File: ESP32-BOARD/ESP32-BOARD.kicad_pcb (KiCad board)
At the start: 2 copper layers, 150 x 99.9 mm, 160 parts, among them J101 Screw_Terminal_01x08, J102 Screw_Terminal_01x08, J103 Screw_Terminal_01x08, J104 Screw_Terminal_01x08, J105 Input_01x02, J106 Screw_Terminal_01x04, J120 Conn_01x07_Male, Q101 BT136-600, Q102 BT136-600, Q103 BT136-600, Q104 BT136-600, U101 LM358, U102 LM358, U103 LM2596S-ADJ, U104 LM2596S-ADJ, U105 TLP290-4, U106 TLP290-4, U107 KAQY212S, U108 KAQY212S, U109 MOC3023S, U110 MOC3023S, U111 MOC3023S, U112 MOC3023S, U113 SIM800L, U114 ESP32-dev-board

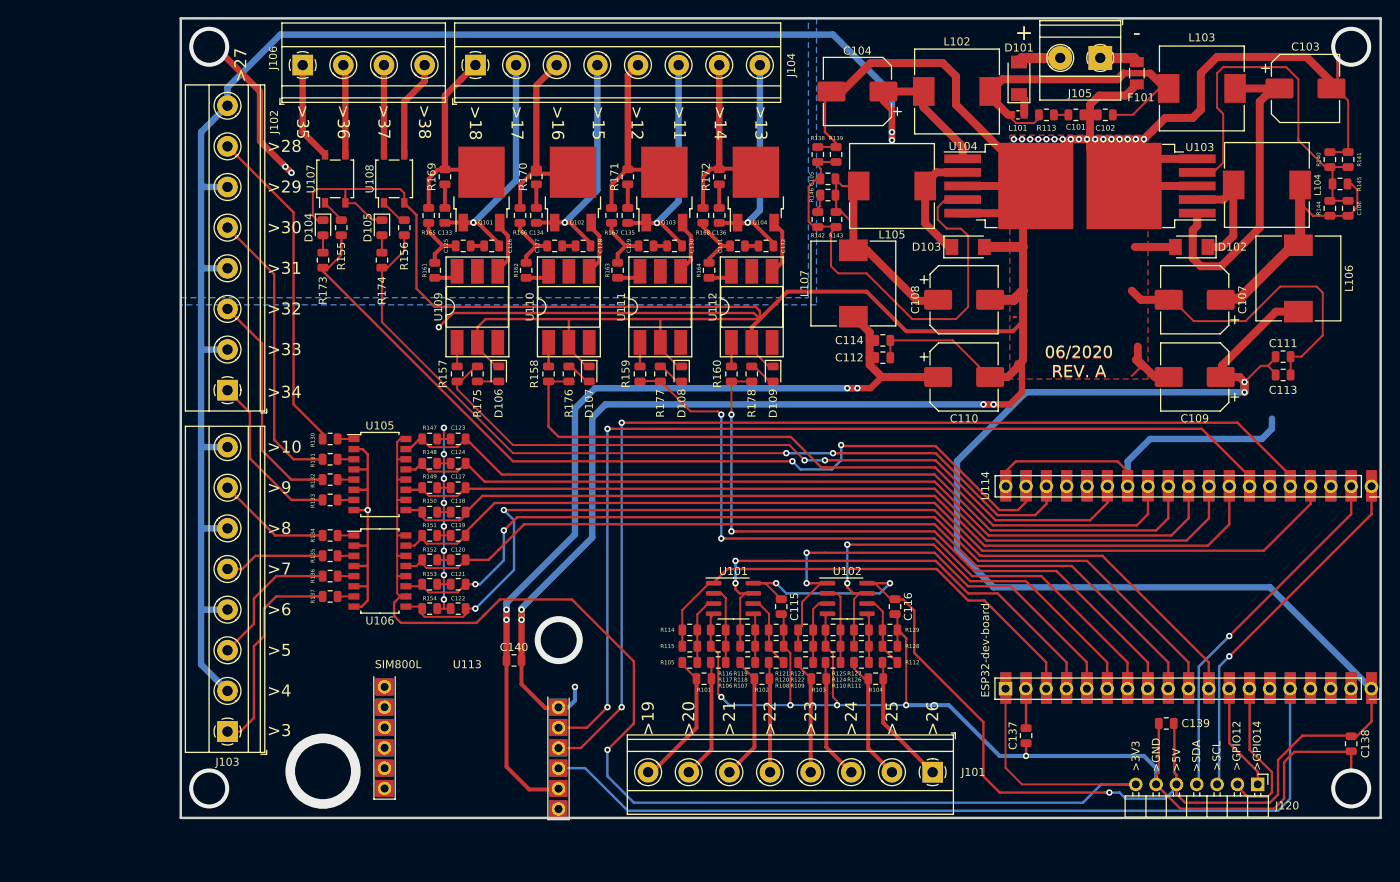
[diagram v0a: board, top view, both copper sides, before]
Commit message: arrumei as dimensoes dos furos
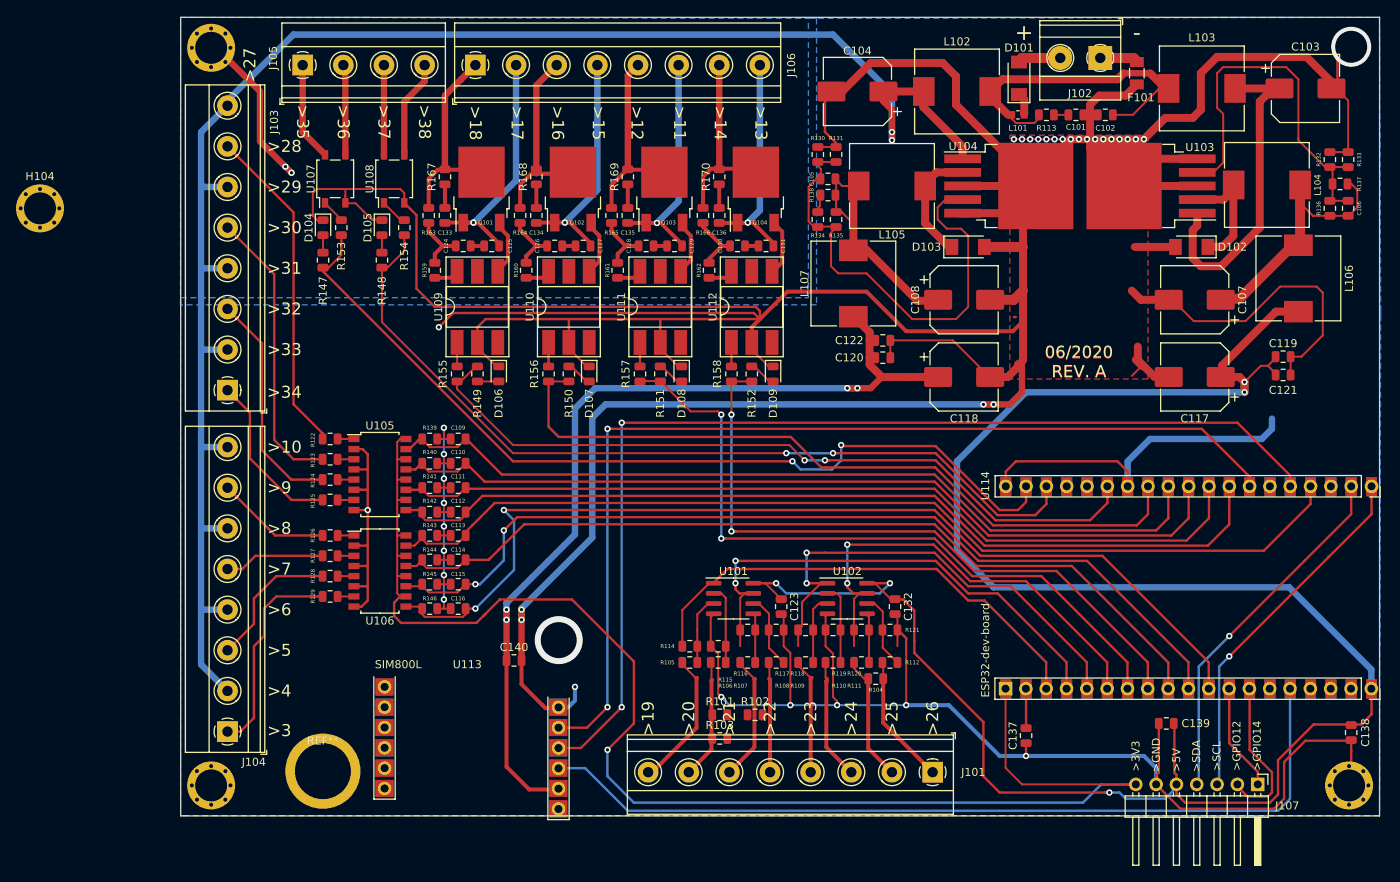
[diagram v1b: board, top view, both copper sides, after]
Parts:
- removed the R114 at (155.1, 119.6)
- removed the R116 at (158.6, 119.6)
- removed the R118 at (162.3, 121.7)
- removed the R120 at (165.9, 121.7)
- removed the R122 at (169.5, 121.7)
- removed the R124 at (173.0, 121.7)
- removed the R126 at (176.5, 121.7)
- removed the R128 at (180.1, 121.7)
- added H101: MountingHole_Pad, e-Power:MountingHole_4mm_Pad_Via, F.Cu at (95.2, 46.9)
- added H102: MountingHole_Pad, e-Power:MountingHole_4mm_Pad_Via, F.Cu at (95.2, 139.1)
- added H103: MountingHole_Pad, e-Power:MountingHole_4mm_Pad_Via, F.Cu at (237.5, 139.1)
- added H104: MountingHole_Pad, e-Power:MountingHole_4mm_Pad_Via, F.Cu at (73.8, 66.9)
- added REF**: MountingHole_3.2mm_M3_DIN965_Pad, e-Power:MountingHole_3.2mm_M3_Pad, F.Cu at (109.2, 137.3)
- R101, R102, R103, R104: value 33R -> 15R
- U107, U108: value KAQY212S -> KAQY214S
- moved R103 14.5 mm to (158.8, 133.2)
- moved R101 4.92 mm to (158.8, 130.2)
- moved R102 4.59 mm to (163.2, 130.2)
- moved C138 1.40 mm to (237.7, 132.5)
- renumbered C123 to C109, C124 to C110, C117 to C111, C118 to C112, C119 to C113, C120 to C114, C121 to C115, C122 to C116, C109 to C117, C110 to C118, C111 to C119, C112 to C120, C113 to C121, C114 to C122, C115 to C123, C125 to C124, C126 to C125, C127 to C126, C128 to C127, C129 to C128, C130 to C129, C131 to C130, C132 to C131, C116 to C132, J105 to J102, J102 to J103, J103 to J104, J106 to J105, J104 to J106, J120 to J107, R115 to R114, R117 to R115, R119 to R116, R121 to R117, R123 to R118, R125 to R119, R127 to R120, R129 to R121, R130 to R122, R131 to R123, R132 to R124, R133 to R125, R134 to R126, R135 to R127, R136 to R128, R137 to R129, R138 to R130, R139 to R131, R140 to R132, R141 to R133, R142 to R134, R143 to R135, R144 to R136, R145 to R137, R146 to R138, R147 to R139, R148 to R140, R149 to R141, R150 to R142, R151 to R143, R152 to R144, R153 to R145, R154 to R146, R173 to R147, R174 to R148, R175 to R149, R176 to R150, R177 to R151, R178 to R152, R155 to R153, R156 to R154, R157 to R155, R158 to R156, R159 to R157, R160 to R158, R161 to R159, R162 to R160, R163 to R161, R164 to R162, R165 to R163, R166 to R164, R167 to R165, R168 to R166, R169 to R167, R170 to R168, R171 to R169, R172 to R170
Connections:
- U101 pad 2: Net-(R106-Pad1) -> Net-(R105-Pad1)
- U101 pad 3: Net-(R105-Pad1) -> Net-(R106-Pad1)
- U101 pad 5: Net-(R107-Pad1) -> Net-(R108-Pad1)
- U101 pad 6: Net-(R108-Pad1) -> Net-(R107-Pad1)
- U102 pad 2: Net-(R110-Pad1) -> Net-(R109-Pad1)
- U102 pad 3: Net-(R109-Pad1) -> Net-(R110-Pad1)
- U102 pad 5: Net-(R111-Pad1) -> Net-(R112-Pad1)
- U102 pad 6: Net-(R112-Pad1) -> Net-(R111-Pad1)
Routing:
- net GND: track 904.7 -> 906.7 mm, vias 44 -> 40
- net +5V: track 263.5 -> 264.6 mm
- net VCC: track 214.8 -> 213.8 mm
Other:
- board size 150 x 99.9 mm -> 149.9 x 99.8 mm

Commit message: changes de boards to 4 layers
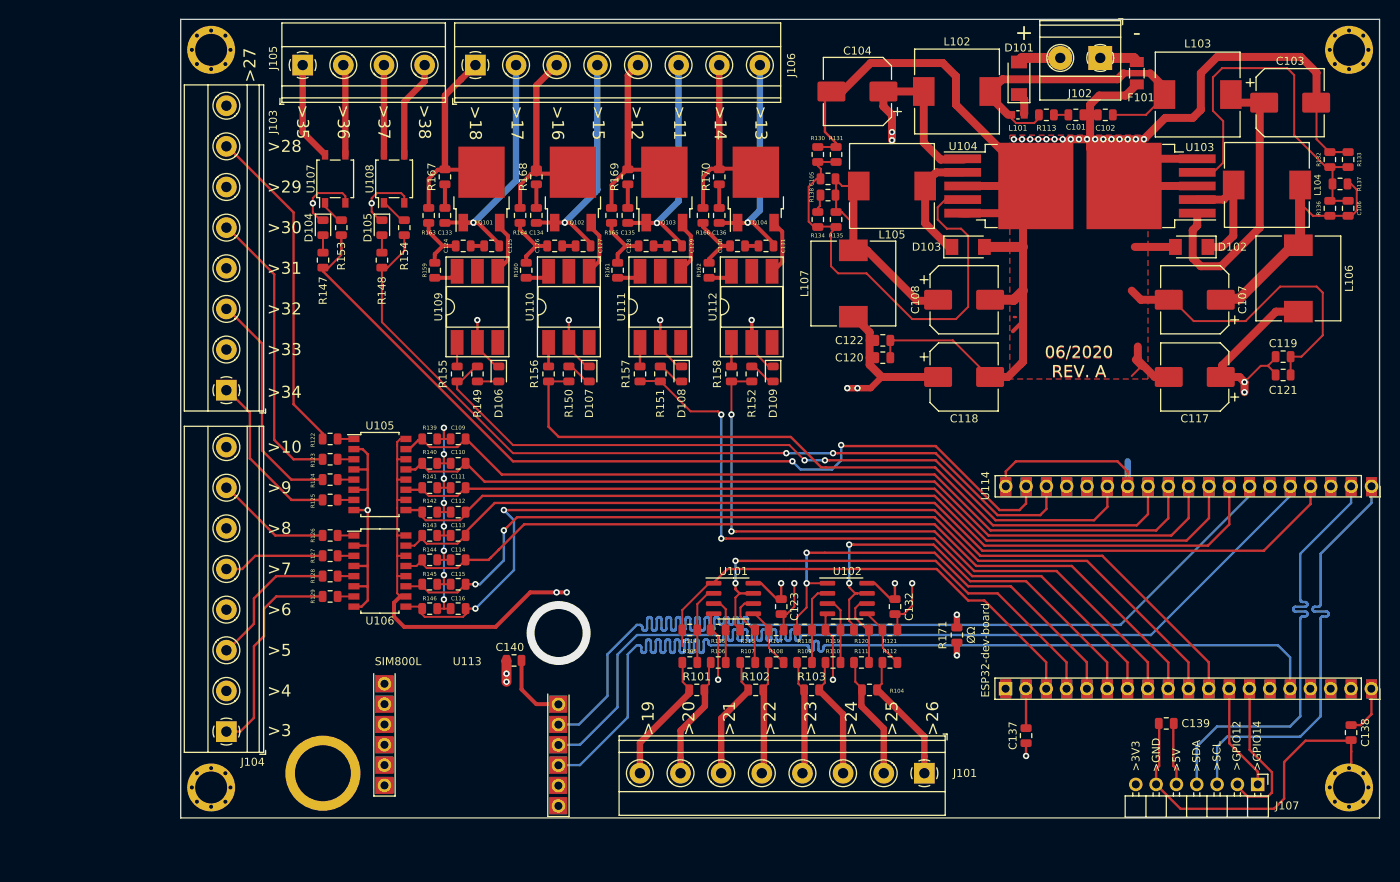
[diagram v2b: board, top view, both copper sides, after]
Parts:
- removed REF**: MountingHole_3.2mm_M3_DIN965_Pad, e-Power:MountingHole_3.2mm_M3_Pad
- added H105: MountingHole_Pad, e-Power:MountingHole_3.2mm_M3_Pad, F.Cu at (109.2, 137.5)
- added R171: 0R, Resistor_SMD:R_0805_2012Metric, F.Cu at (188.5, 120.3)
- moved H104 164.8 mm to (237.5, 47.1)
- moved R103 13.0 mm to (170.3, 127.1)
- moved R101 4.24 mm to (155.9, 127.1)
- moved R102 3.11 mm to (163.3, 127.1)
- moved C103 2.62 mm to (230.1, 53.7)
- moved R115 2.03 mm to (158.6, 119.6)
- moved R114 2.03 mm to (155.1, 119.6)
- moved R104 1.60 mm to (177.5, 127.1)
- moved J101 1.04 mm to (184.4, 137.5)
- moved L103 0.92 mm to (218.6, 52.7)
- moved U113 0.38 mm to (138.7, 141.6)
- moved H101 0.25 mm to (95.2, 47.1)
- moved H102 0.25 mm to (95.2, 139.3)
- moved H103 0.25 mm to (237.5, 139.3)
- moved J103 0.14 mm to (97.1, 89.7)
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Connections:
- C138 pad 1: +5V -> /5V_u
- C139 pad 1: +5V -> /5V_u
- J107 pad 5: +5V -> /5V_u
- U114 pad 19: +5V -> /5V_u
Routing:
- net GND: track 906.7 -> 509.4 mm, vias 40 -> 37
- net +5V: track 264.6 -> 133.9 mm
- net /5V_u: track 0.00 -> 116.5 mm, vias 0 -> 1
- net /RST_SIM800L: track 108.0 -> 130.0 mm
- net +3V3: track 176.9 -> 165.9 mm, vias 1 -> 2
- net /SDA: track 45.3 -> 55.4 mm, vias 1 -> 0
- net /SCL: track 45.3 -> 54.2 mm, vias 1 -> 0
- net 4.1V: track 116.1 -> 107.4 mm
- net Net-(R107-Pad1): track 6.22 -> 10.2 mm
- net /TX_SIM800L: track 125.9 -> 129.8 mm, vias 2 -> 0
- net /RX_SIM800L: track 133.2 -> 129.8 mm, vias 2 -> 0
- net Net-(R111-Pad1): track 6.46 -> 9.54 mm
- net VCC: track 213.8 -> 216.6 mm
- net /CURR_03: track 60.8 -> 58.1 mm
- net /CURR_04: track 58.4 -> 56.2 mm
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- added copper zone on In1.Cu(GND), net GND
- removed copper zone on B.Cu, net GND
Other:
- copper layers 2 -> 4
- board text added: "ØΩ"

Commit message: updates related to review B
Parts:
- moved J103 0.63 mm to (97.8, 89.7)
- moved J104 0.63 mm to (97.8, 132.3)
- moved H101 0.51 mm to (95.7, 47.1)
- moved H102 0.51 mm to (95.7, 139.3)
- moved H103 0.51 mm to (238.0, 139.3)
- moved H104 0.51 mm to (238.0, 47.1)
- moved C117 0.37 mm to (217.9, 88.3)
- moved J101 0.26 mm to (184.4, 137.3)
- moved J102 0.25 mm to (206.4, 48.4)
- moved U113 0.25 mm to (138.7, 141.4)
- moved J106 0.13 mm to (128.3, 49.1)
- moved J105 0.13 mm to (106.7, 49.1)
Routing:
- net GND: track 509.4 -> 485.6 mm
- net /CURR_01: track 60.3 -> 58.4 mm
- net /5V_u: track 116.5 -> 115.6 mm
- net VCC: track 216.6 -> 217.3 mm
- net Net-(J103-Pad3): track 29.1 -> 29.6 mm
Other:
- outline, holes or cut-outs redrawn
- board text added: "07/2020 REV. B"
- board text added: "ESP32 dev-board"
- board text added: "SIM800L"
- board text removed: "06/2020 REV. A"

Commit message: update on project
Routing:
- net GND: vias 37 -> 207

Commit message: modificacoes na placa
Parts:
- removed C124, C125, C126, C127, C128, C129, C130, C131: 100nF, Capacitor_SMD:C_0805_2012Metric
- removed C133, C134, C135, C136: 10nF, Capacitor_SMD:C_0805_2012Metric
- removed D104, D105: LED, LED_SMD:LED_0805_2012Metric
- removed Q101, Q102, Q103, Q104: BT136-600, Package_TO_SOT_SMD:TO-252-2
- removed R147, R148, R159, R160, R161, R162: 330R, Resistor_SMD:R_0805_2012Metric
- removed R153, R154, R155, R156, R157, R158: 100R, Resistor_SMD:R_0805_2012Metric
- removed R163, R164, R165, R166: 470R, Resistor_SMD:R_0805_2012Metric
- removed R167, R168, R169, R170: 39R, Resistor_SMD:R_0805_2012Metric
- removed U107, U108: KAQY214S, Package_SO:SO-4_4.4x4.3mm_P2.54mm
- removed U109, U110, U111, U112: MOC3023S, Package_DIP:DIP-6_W8.89mm_SMDSocket_LongPads
- added D10: SS54HF, e-Power:DO-214AC, F.Cu at (109.5, 84.5)
- added D11: SS54HF, e-Power:DO-214AC, F.Cu at (118.9, 84.5)
- added D12: SS54HF, e-Power:DO-214AC, F.Cu at (129.8, 84.5)
- added D13: SS54HF, e-Power:DO-214AC, F.Cu at (139.9, 84.5)
- added D14: SS54HF, e-Power:DO-214AC, F.Cu at (150.1, 84.5)
- added D15: SS54HF, e-Power:DO-214AC, F.Cu at (160.3, 84.5)
- added D4: LED, LED_SMD:LED_0805_2012Metric, F.Cu at (114.5, 87.0)
- added D5: LED, LED_SMD:LED_0805_2012Metric, F.Cu at (124.4, 87.0)
- added F1: Fuse, e-Power:FUSE_1206_3216Metric, F.Cu at (196.6, 91.6)
- added F2: Fuse, e-Power:FUSE_1206_3216Metric, F.Cu at (199.4, 91.6)
- added F4: Fuse, e-Power:FUSE_1206_3216Metric, F.Cu at (202.2, 91.6)
- added F5: Fuse, e-Power:FUSE_1206_3216Metric, F.Cu at (205.0, 91.6)
- added J8: DHT11, Connector_PinHeader_2.54mm:PinHeader_1x04_P2.54mm_Vertical, F.Cu at (202.2, 138.8)
- added K1: G5NB-1A-E, e-Power:Relay_SPST_Omron-G5Q-1A, F.Cu at (117.5, 79.3)
- added K2: G5NB-1A-E, e-Power:Relay_SPST_Omron-G5Q-1A, F.Cu at (126.7, 79.4)
- added K3: G5NB-1A-E, e-Power:Relay_SPST_Omron-G5Q-1A, F.Cu at (137.5, 79.4)
- added K4: G5NB-1A-E, e-Power:Relay_SPST_Omron-G5Q-1A, F.Cu at (147.8, 79.4)
- added K5: G5NB-1A-E, e-Power:Relay_SPST_Omron-G5Q-1A, F.Cu at (157.8, 79.4)
- added K6: G5NB-1A-E, e-Power:Relay_SPST_Omron-G5Q-1A, F.Cu at (168.0, 79.4)
- added Q1: MMBT5551, Package_TO_SOT_SMD:SOT-23, F.Cu at (113.3, 83.2)
- added Q2: MMBT5551, Package_TO_SOT_SMD:SOT-23, F.Cu at (122.7, 83.2)
- added Q3: MMBT5551, Package_TO_SOT_SMD:SOT-23, F.Cu at (133.6, 83.2)
- added Q4: MMBT5551, Package_TO_SOT_SMD:SOT-23, F.Cu at (143.8, 83.2)
- added Q5: MMBT5551, Package_TO_SOT_SMD:SOT-23, F.Cu at (153.9, 83.2)
- added Q6: MMBT5551, Package_TO_SOT_SMD:SOT-23, F.Cu at (164.1, 83.2)
- added R48: 330R, Resistor_SMD:R_0805_2012Metric, F.Cu at (114.5, 90.6)
- added R49: 330R, Resistor_SMD:R_0805_2012Metric, F.Cu at (124.4, 90.6)
- added R54: 1K, Resistor_SMD:R_0805_2012Metric, F.Cu at (112.3, 87.0)
- added R55: 1K, Resistor_SMD:R_0805_2012Metric, F.Cu at (121.9, 87.0)
- added R56: 1K, Resistor_SMD:R_0805_2012Metric, F.Cu at (132.8, 87.0)
- added R57: 1K, Resistor_SMD:R_0805_2012Metric, F.Cu at (142.7, 87.0)
- added R58: 1K, Resistor_SMD:R_0805_2012Metric, F.Cu at (152.9, 87.0)
- added R59: 1K, Resistor_SMD:R_0805_2012Metric, F.Cu at (163.1, 87.0)
- added R60: 1K, Resistor_SMD:R_0805_2012Metric, F.Cu at (203.7, 130.4)
- moved R50 7.44 mm to (135.4, 90.6), turned to 270 degrees
- moved R51 5.85 mm to (145.0, 90.6)
- moved R52 4.79 mm to (155.2, 90.6)
- moved D6 4.23 mm to (135.4, 87.0)
- moved R53 3.86 mm to (165.3, 90.6)
- moved R15 3.67 mm to (158.7, 119.6)
- moved R14 3.56 mm to (155.1, 119.6)
- moved C21 2.72 mm to (198.4, 130.4), turned to 180 degrees
- moved D7 2.61 mm to (145.0, 87.0)
- moved J6 1.51 mm to (108.2, 49.1)
- moved D8 1.30 mm to (155.2, 87.0)
- moved J7 1.27 mm to (129.5, 49.1)
- moved C26 0.89 mm to (214.6, 130.4)
- moved D9 0.65 mm to (165.3, 87.0)
- moved C22 0.51 mm to (237.7, 133.0), turned to 90 degrees
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- renumbered C101 to C1, C110 to C10, C111 to C11, C112 to C12, C113 to C13, C114 to C14, C115 to C15, C116 to C16, C117 to C17, C118 to C18, C119 to C19, C102 to C2, C120 to C20, C137 to C21, C138 to C22, C121 to C23, C122 to C24, C123 to C25, C139 to C26, C140 to C27, C132 to C28, C103 to C3, C104 to C4, C105 to C5, C106 to C6, C107 to C7, C108 to C8, C109 to C9, D101 to D1, D102 to D2, D103 to D3, D106 to D6, D107 to D7, D108 to D8, D109 to D9, F101 to F3, H101 to H1, H102 to H2, H103 to H3, H104 to H4, H105 to H5, J101 to J1, J102 to J2, J103 to J3, J104 to J4, J107 to J5, J105 to J6, J106 to J7, L101 to L1, L102 to L2, L103 to L3, L104 to L4, L105 to L5, L106 to L6, L107 to L7, R101 to R1, R110 to R10, R111 to R11, R112 to R12, R113 to R13, R115 to R14, R114 to R15, R116 to R16, R117 to R17, R118 to R18, R119 to R19, R102 to R2, R120 to R20, R121 to R21, R122 to R22, R123 to R23, R124 to R24, R125 to R25, R126 to R26, R127 to R27, R128 to R28, R129 to R29, R103 to R3, R130 to R30, R131 to R31, R132 to R32, R133 to R33, R134 to R34, R135 to R35, R136 to R36, R137 to R37, R138 to R38, R139 to R39, R104 to R4, R140 to R40, R141 to R41, R142 to R42, R143 to R43, R144 to R44, R145 to R45, R146 to R46, R171 to R47, R105 to R5, R149 to R50, R150 to R51, R151 to R52, R152 to R53, R106 to R6, R107 to R7, R108 to R8, R109 to R9, U101 to U1, U102 to U2, U103 to U3, U104 to U4, U105 to U5, U106 to U6, U113 to U7, U114 to U8
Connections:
- C22 pad 1: /5V_u -> GND
- C22 pad 2: GND -> /5V_u
- J1 pad 1: Net-(J101-Pad1) -> GND
- J1 pad 2: Net-(J101-Pad2) -> Net-(J1-Pad2)
- J1 pad 3: Net-(J101-Pad3) -> GND
- J1 pad 4: Net-(J101-Pad4) -> Net-(J1-Pad4)
- J1 pad 5: Net-(J101-Pad5) -> GND
- J1 pad 6: Net-(J101-Pad6) -> Net-(J1-Pad6)
- J1 pad 7: Net-(J101-Pad7) -> GND
- J1 pad 8: Net-(J101-Pad8) -> Net-(J1-Pad8)
- R1 pad 1: Net-(J101-Pad8) -> GND
- R1 pad 2: Net-(J101-Pad7) -> Net-(J1-Pad8)
- R10 pad 2: Net-(J101-Pad3) -> Net-(J1-Pad4)
- R11 pad 2: Net-(J101-Pad2) -> GND
- R12 pad 2: Net-(J101-Pad1) -> Net-(J1-Pad2)
- R14 pad 1: GND -> /CURR_01
- R14 pad 2: Net-(R106-Pad1) -> Net-(R14-Pad2)
- R15 pad 1: Net-(R105-Pad1) -> Net-(R15-Pad1)
- R15 pad 2: /CURR_01 -> GND
- R2 pad 1: Net-(J101-Pad6) -> GND
- R2 pad 2: Net-(J101-Pad5) -> Net-(J1-Pad6)
- R3 pad 1: Net-(J101-Pad4) -> GND
- R3 pad 2: Net-(J101-Pad3) -> Net-(J1-Pad4)
- R4 pad 1: Net-(J101-Pad2) -> GND
- R4 pad 2: Net-(J101-Pad1) -> Net-(J1-Pad2)
- R5 pad 1: Net-(R105-Pad1) -> Net-(R14-Pad2)
- R5 pad 2: Net-(J101-Pad8) -> GND
- R6 pad 1: Net-(R106-Pad1) -> Net-(R15-Pad1)
- R6 pad 2: Net-(J101-Pad7) -> Net-(J1-Pad8)
- R7 pad 2: Net-(J101-Pad6) -> GND
- R8 pad 2: Net-(J101-Pad5) -> Net-(J1-Pad6)
- R9 pad 2: Net-(J101-Pad4) -> GND
- U1 pad 2: Net-(R105-Pad1) -> Net-(R14-Pad2)
- U1 pad 3: Net-(R106-Pad1) -> Net-(R15-Pad1)
- U8 pad 34: Net-(U114-Pad34) -> /DHT11
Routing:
- net +5V: track 133.9 -> 277.5 mm
- net /DHT11: track 0.00 -> 54.9 mm, vias 0 -> 1
- net Net-(J7-Pad3): track 36.3 -> 13.9 mm
- net +3V3: track 166.4 -> 186.2 mm, vias 2 -> 3
- net /OUT_2: track 108.5 -> 88.8 mm
- net Net-(J1-Pad8): track 0.00 -> 17.4 mm
- net Net-(J101-Pad8): track 17.0 -> 0.00 mm
- net Net-(J7-Pad2): track 37.6 -> 20.8 mm, vias 1 -> 0
- net Net-(J101-Pad1): track 16.3 -> 0.00 mm
- net Net-(J1-Pad6): track 0.00 -> 15.8 mm
- net Net-(J101-Pad3): track 15.6 -> 0.00 mm
- net Net-(J101-Pad7): track 15.6 -> 0.00 mm
- net Net-(J101-Pad2): track 15.4 -> 0.00 mm
- net Net-(J101-Pad6): track 15.3 -> 0.00 mm
- net Net-(J1-Pad4): track 0.00 -> 15.3 mm
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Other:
- board text added: "11/2020 REV. B"
- board text added: ">GPIO3"
- board text added: ">NC"
- board text removed: "07/2020 REV. B"
